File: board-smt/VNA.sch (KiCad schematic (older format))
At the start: 93 parts, among them J1 Conn_02x07_Odd_Even, J10 Conn_01x01, J11 Conn_01x01, J12 Conn_01x01, J13 Barrel_Jack, J14 Conn_01x01, J15 Conn_02x05_Odd_Even, J16 Conn_01x01, J17 Conn_01x04, J18 Conn_01x01, J19 Conn_01x01, J2 Conn_Coaxial, J20 Conn_01x01, J21 Conn_01x01, J22 Conn_01x02, J23 Conn_01x02, J24 USB_B, J25 Conn_01x02, J3 Conn_01x01, J4 Conn_01x01, J5 Conn_01x01, J6 Conn_01x01, J7 Conn_01x01, J8 Conn_01x01, J9 Conn_Coaxial, Q3 S9018, U1 SI5351A, U10 MT3608, U8 AMS1117-3V3, U9 78M05_TO252, Y1 27 MHz

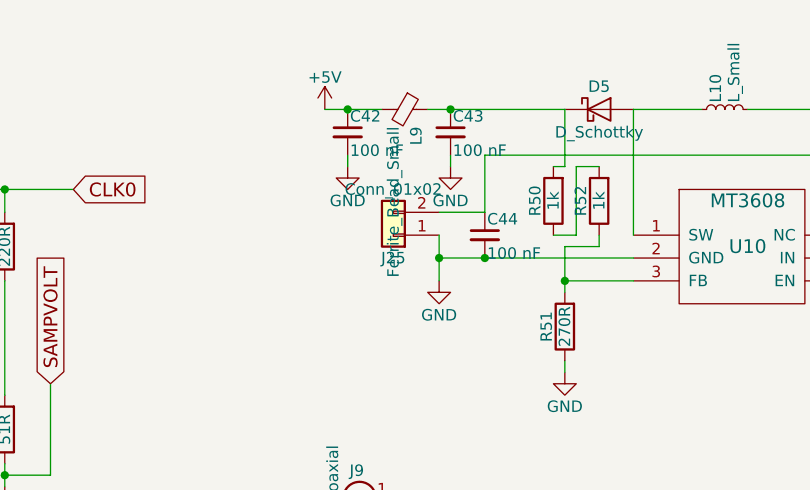
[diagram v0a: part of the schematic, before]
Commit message: 100 uH in pi filter
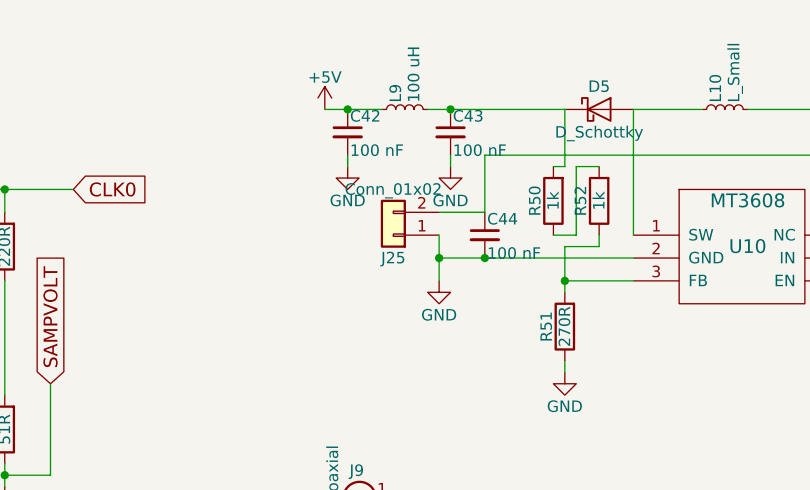
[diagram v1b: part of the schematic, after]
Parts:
- removed L9: Ferrite_Bead_Small, Inductors_SMD:L_1206_HandSoldering, symbol Ferrite_Bead_Small
- added L9: 100 uH, Inductors_SMD:L_1206_HandSoldering, symbol L_Small
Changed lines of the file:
@@
 Wire Wire Line
 	4800 800  5050 800
-$Comp
-L Ferrite_Bead_Small L9
-U 1 1 5DCD25CB
-P 5150 800
-F 0 "L9" H 5225 850 50  0000 L CNN
-F 1 "Ferrite_Bead_Small" H 5225 750 50  0000 L CNN
-F 2 "Inductors_SMD:L_1206_HandSoldering" V 5080 800 50  0001 C CNN
-F 3 "" H 5150 800 50  0001 C CNN
-	1    5150 800
-	0    1    1    0
-$EndComp
 Connection ~ 4900 800
 $Comp
@@
 	6000 1400 6000 1350
 Connection ~ 5850 1550
+$Comp
+L L_Small L9
+U 1 1 5DCCE487
+P 5150 800
+F 0 "L9" H 5180 840 50  0000 L CNN
+F 1 "100 uH" H 5180 760 50  0000 L CNN
+F 2 "Inductors_SMD:L_1206_HandSoldering" H 5150 800 50  0001 C CNN
+F 3 "" H 5150 800 50  0001 C CNN
+	1    5150 800
+	0    -1   -1   0
+$EndComp
 $EndSCHEMATC

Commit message: Rearranged the PCB, CN3502 battery charger and MT3608 boost converter on-board
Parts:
- removed C38, C44: 100 nF, Capacitors_SMD:C_0805_HandSoldering, symbol C_Small
- removed J15: Conn_02x05_Odd_Even, Pin_Headers:Pin_Header_Straight_2x05_Pitch2.54mm, symbol Conn_02x05_Odd_Even
- removed J25: Conn_01x02, Connectors_Molex:Molex_KK-6410-02_02x2.54mm_Straight, symbol Conn_01x02
- added C38, C44: 22 uF, Capacitors_SMD:CP_Elec_4x4.5, symbol CP
- added C45: 4.7 uF, Capacitors_SMD:CP_Elec_4x4.5, symbol CP
- added C49: 10 uF, Capacitors_SMD:CP_Elec_4x4.5, symbol CP
- added D6, D7: LED, LEDs:LED_0805, symbol LED
- added J15: Conn_01x03, Connectors_Molex:Molex_KK-6410-03_03x2.54mm_Straight, symbol Conn_01x03
- added JP6: Jumper_NC_Small, Pin_Headers:Pin_Header_Straight_1x02_Pitch2.54mm, symbol Jumper_NC_Small
- added R53: DIV1, Resistors_SMD:R_0805_HandSoldering, symbol R
- added R54: DIV2, Resistors_SMD:R_0805_HandSoldering, symbol R
- added R55: ISET, Resistors_SMD:R_0805_HandSoldering, symbol R
- added R56, R57: 270R, Resistors_SMD:R_0805_HandSoldering, symbol R
- added SW1: SW_DPDT_x2, Connectors_Molex:Molex_KK-6410-06_06x2.54mm_Straight, symbol SW_DPDT_x2
- added U11: CN3052, Housings_SOIC:SOIC-8_3.9x4.9mm_Pitch1.27mm, symbol CN3052
- L9: footprint Inductors_SMD:L_1206_HandSoldering -> Inductors_SMD:L_7.3x7.3_H4.5
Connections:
- net labels added: REG5VOUT
- wire segments 273 -> 304
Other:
- moved on the sheet: C42, C43, D3, D4, D5, J9, L10, L9, R17, R18, R50, R51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

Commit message: Move components around on board, adjusted fixture, added touchscreen disables
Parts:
- removed D6: LED, LEDs:LED_0805, symbol LED
- removed J15: Conn_01x03, Connectors_Molex:Molex_KK-6410-03_03x2.54mm_Straight, symbol Conn_01x03
- removed J23: Conn_01x02, Connectors_Molex:Molex_KK-6410-02_02x2.54mm_Straight, symbol Conn_01x02
- removed R54: DIV2, Resistors_SMD:R_0805_HandSoldering, symbol R
- removed R56: 270R, Resistors_SMD:R_0805_HandSoldering, symbol R
- added J15: Conn_01x02, Connectors_Molex:Molex_KK-6410-02_02x2.54mm_Straight, symbol Conn_01x02
- R53: value DIV1 -> 10k
- R55: value ISET -> 4k7
- Y1: footprint Crystals:Crystal_HC49-U_Vertical -> Crystals:Crystal_SMD_3225-4pin_3.2x2.5mm_HandSoldering
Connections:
- net labels added: POWFILT
- wire segments 304 -> 291
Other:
- moved on the sheet: C42, C43, L9

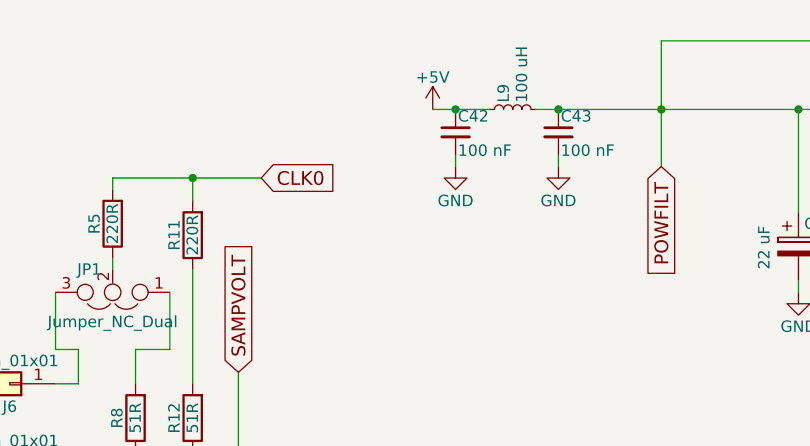
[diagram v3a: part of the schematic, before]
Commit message: Added protection Zener diode on Pi filter to protect against ON/OFF transients
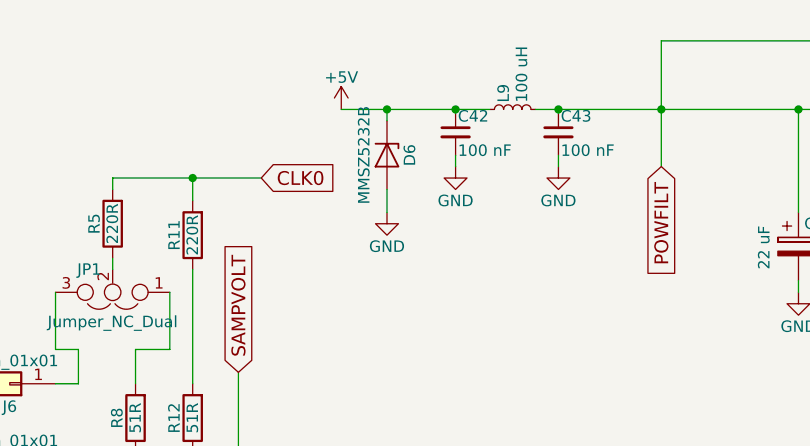
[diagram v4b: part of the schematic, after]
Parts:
- added D6: MMSZ5232B, Diodes_SMD:D_SOD-123, symbol D_Zener
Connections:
- net +5V: now also D6.1 (K)
- net GND: now also D6.2 (A)
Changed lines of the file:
@@
 $EndComp
 $Comp
-L +3V3 #PWR35
+L +3V3 #PWR36
 U 1 1 5BB1752D
 P 5700 5700
-F 0 "#PWR35" H 5700 5550 50  0001 C CNN
+F 0 "#PWR36" H 5700 5550 50  0001 C CNN
 F 1 "+3V3" H 5700 5840 50  0000 C CNN
 F 2 "" H 5700 5700 50  0001 C CNN
@@
 SYNCSAMPLE
 $Comp
-L +5V #PWR55
+L +5V #PWR56
 U 1 1 5BB2CE22
 P 9550 4200
-F 0 "#PWR55" H 9550 4050 50  0001 C CNN
+F 0 "#PWR56" H 9550 4050 50  0001 C CNN
 F 1 "+5V" H 9550 4340 50  0000 C CNN
 F 2 "" H 9550 4200 50  0001 C CNN
@@
 $EndComp
 $Comp
-L GND #PWR38
+L GND #PWR39
 U 1 1 5BB2D2D6
 P 6000 6000
-F 0 "#PWR38" H 6000 5750 50  0001 C CNN
+F 0 "#PWR39" H 6000 5750 50  0001 C CNN
 F 1 "GND" H 6000 5850 50  0000 C CNN
 F 2 "" H 6000 6000 50  0001 C CNN
@@
 $EndComp
 $Comp
-L GND #PWR36
+L GND #PWR37
 U 1 1 5BB350C1
 P 5750 3400
-F 0 "#PWR36" H 5750 3150 50  0001 C CNN
+F 0 "#PWR37" H 5750 3150 50  0001 C CNN
 F 1 "GND" H 5750 3250 50  0000 C CNN
 F 2 "" H 5750 3400 50  0001 C CNN
@@
 $EndComp
 $Comp
-L +5V #PWR59
+L +5V #PWR60
 U 1 1 5BB3F764
 P 10550 5200
-F 0 "#PWR59" H 10550 5050 50  0001 C CNN
+F 0 "#PWR60" H 10550 5050 50  0001 C CNN
 F 1 "+5V" H 10550 5340 50  0000 C CNN
 F 2 "" H 10550 5200 50  0001 C CNN
@@
 $EndComp
 $Comp
-L GND #PWR61
+L GND #PWR62
 U 1 1 5BB3F96D
 P 10850 5900
-F 0 "#PWR61" H 10850 5650 50  0001 C CNN
+F 0 "#PWR62" H 10850 5650 50  0001 C CNN
 F 1 "GND" H 10850 5750 50  0000 C CNN
 F 2 "" H 10850 5900 50  0001 C CNN
@@
 $EndComp
 $Comp
-L GND #PWR62
+L GND #PWR63
 U 1 1 5BB37FFB
 P 11200 4650
-F 0 "#PWR62" H 11200 4400 50  0001 C CNN
+F 0 "#PWR63" H 11200 4400 50  0001 C CNN
 F 1 "GND" H 11200 4500 50  0000 C CNN
 F 2 "" H 11200 4650 50  0001 C CNN
@@
 $EndComp
 $Comp
-L +5V #PWR56
+L +5V #PWR57
 U 1 1 5BB381D0
 P 10100 2650
-F 0 "#PWR56" H 10100 2500 50  0001 C CNN
+F 0 "#PWR57" H 10100 2500 50  0001 C CNN
 F 1 "+5V" H 10100 2790 50  0000 C CNN
 F 2 "" H 10100 2650 50  0001 C CNN
@@
 $EndComp
 $Comp
-L GND #PWR32
+L GND #PWR33
 U 1 1 5BE16D13
 P 4800 3050
-F 0 "#PWR32" H 4800 2800 50  0001 C CNN
+F 0 "#PWR33" H 4800 2800 50  0001 C CNN
 F 1 "GND" H 4800 2900 50  0000 C CNN
 F 2 "" H 4800 3050 50  0001 C CNN
@@
 $EndComp
 $Comp
-L GND #PWR27
+L GND #PWR28
 U 1 1 5BFEB64E
 P 4050 5600
-F 0 "#PWR27" H 4050 5350 50  0001 C CNN
+F 0 "#PWR28" H 4050 5350 50  0001 C CNN
 F 1 "GND" H 4050 5450 50  0000 C CNN
 F 2 "" H 4050 5600 50  0001 C CNN
@@
 $EndComp
 $Comp
-L GND #PWR31
+L GND #PWR32
 U 1 1 5BFEBC91
 P 4750 5600
-F 0 "#PWR31" H 4750 5350 50  0001 C CNN
+F 0 "#PWR32" H 4750 5350 50  0001 C CNN
 F 1 "GND" H 4750 5450 50  0000 C CNN
 F 2 "" H 4750 5600 50  0001 C CNN
@@
 $EndComp
 $Comp
-L GND #PWR34
+L GND #PWR35
 U 1 1 5C1BDCBD
 P 5150 6200
-F 0 "#PWR34" H 5150 5950 50  0001 C CNN
+F 0 "#PWR35" H 5150 5950 50  0001 C CNN
 F 1 "GND" H 5150 6050 50  0000 C CNN
 F 2 "" H 5150 6200 50  0001 C CNN
@@
 $EndComp
 $Comp
-L GND #PWR53
+L GND #PWR54
 U 1 1 5C258D29
 P 9350 3900
-F 0 "#PWR53" H 9350 3650 50  0001 C CNN
+F 0 "#PWR54" H 9350 3650 50  0001 C CNN
 F 1 "GND" H 9350 3750 50  0000 C CNN
 F 2 "" H 9350 3900 50  0001 C CNN
@@
 $EndComp
 $Comp
-L GND #PWR37
+L GND #PWR38
 U 1 1 5C25906A
 P 5800 6050
-F 0 "#PWR37" H 5800 5800 50  0001 C CNN
+F 0 "#PWR38" H 5800 5800 50  0001 C CNN
 F 1 "GND" H 5800 5900 50  0000 C CNN
 F 2 "" H 5800 6050 50  0001 C CNN
@@
 $EndComp
 $Comp
-L GND #PWR50
+L GND #PWR51
 U 1 1 5D1ABD6C
 P 9150 3400
-F 0 "#PWR50" H 9150 3150 50  0001 C CNN
+F 0 "#PWR51" H 9150 3150 50  0001 C CNN
 F 1 "GND" H 9150 3250 50  0000 C CNN
 F 2 "" H 9150 3400 50  0001 C CNN
@@
 $EndComp
 $Comp
-L +5V #PWR49
+L +5V #PWR50
 U 1 1 5D1AC0C3
 P 8800 2900
-F 0 "#PWR49" H 8800 2750 50  0001 C CNN
+F 0 "#PWR50" H 8800 2750 50  0001 C CNN
 F 1 "+5V" H 8800 3040 50  0000 C CNN
 F 2 "" H 8800 2900 50  0001 C CNN
@@
 $EndComp
 $Comp
-L GND #PWR54
+L GND #PWR55
 U 1 1 5D1ACA17
 P 9550 3650
-F 0 "#PWR54" H 9550 3400 50  0001 C CNN
+F 0 "#PWR55" H 9550 3400 50  0001 C CNN
 F 1 "GND" H 9550 3500 50  0000 C CNN
 F 2 "" H 9550 3650 50  0001 C CNN
@@
 $EndComp
 $Comp
-L GND #PWR29
+L GND #PWR30
 U 1 1 5D91A3E2
 P 4450 6550
-F 0 "#PWR29" H 4450 6300 50  0001 C CNN
+F 0 "#PWR30" H 4450 6300 50  0001 C CNN
 F 1 "GND" H 4450 6400 50  0000 C CNN
 F 2 "" H 4450 6550 50  0001 C CNN
@@
 NoConn ~ 10350 4350
 $Comp
-L +5V #PWR58
+L +5V #PWR59
 U 1 1 5DB1C7B8
 P 10200 4500
-F 0 "#PWR58" H 10200 4350 50  0001 C CNN
+F 0 "#PWR59" H 10200 4350 50  0001 C CNN
 F 1 "+5V" H 10200 4640 50  0000 C CNN
 F 2 "" H 10200 4500 50  0001 C CNN
@@
 $EndComp
 $Comp
-L GND #PWR48
+L GND #PWR49
 U 1 1 5DCC5E0A
 P 8650 6300
-F 0 "#PWR48" H 8650 6050 50  0001 C CNN
+F 0 "#PWR49" H 8650 6050 50  0001 C CNN
 F 1 "GND" H 8650 6150 50  0000 C CNN
 F 2 "" H 8650 6300 50  0001 C CNN
@@
 $EndComp
 $Comp
-L GND #PWR60
+L GND #PWR61
 U 1 1 5DCC6B2E
 P 10600 6450
-F 0 "#PWR60" H 10600 6200 50  0001 C CNN
+F 0 "#PWR61" H 10600 6200 50  0001 C CNN
 F 1 "GND" H 10600 6300 50  0000 C CNN
 F 2 "" H 10600 6450 50  0001 C CNN
@@
 $EndComp
 $Comp
-L GND #PWR33
+L GND #PWR34
 U 1 1 5DCD10CA
 P 5000 1100
-F 0 "#PWR33" H 5000 850 50  0001 C CNN
+F 0 "#PWR34" H 5000 850 50  0001 C CNN
 F 1 "GND" H 5000 950 50  0000 C CNN
 F 2 "" H 5000 1100 50  0001 C CNN
@@
 $EndComp
 $Comp
-L +5V #PWR28
+L +5V #PWR27
 U 1 1 5DCD163E
-P 4450 850
-F 0 "#PWR28" H 4450 700 50  0001 C CNN
-F 1 "+5V" H 4450 990 50  0000 C CNN
-F 2 "" H 4450 850 50  0001 C CNN
-F 3 "" H 4450 850 50  0001 C CNN
-	1    4450 850
+P 4050 850
+F 0 "#PWR27" H 4050 700 50  0001 C CNN
+F 1 "+5V" H 4050 990 50  0000 C CNN
+F 2 "" H 4050 850 50  0001 C CNN
+F 3 "" H 4050 850 50  0001 C CNN
+	1    4050 850
 	1    0    0    -1
 $EndComp
@@
 $EndComp
 $Comp
-L GND #PWR30
+L GND #PWR31
 U 1 1 5DCD1D7F
 P 4550 1100
-F 0 "#PWR30" H 4550 850 50  0001 C CNN
+F 0 "#PWR31" H 4550 850 50  0001 C CNN
 F 1 "GND" H 4550 950 50  0000 C CNN
 F 2 "" H 4550 1100 50  0001 C CNN
@@
 $EndComp
 $Comp
-L GND #PWR46
+L GND #PWR47
 U 1 1 5DCDAD80
 P 8100 1300
-F 0 "#PWR46" H 8100 1050 50  0001 C CNN
+F 0 "#PWR47" H 8100 1050 50  0001 C CNN
 F 1 "GND" H 8100 1150 50  0000 C CNN
 F 2 "" H 8100 1300 50  0001 C CNN
@@
 $EndComp
 $Comp
-L GND #PWR40
+L GND #PWR41
 U 1 1 5DCDB2D2
 P 6450 2000
-F 0 "#PWR40" H 6450 1750 50  0001 C CNN
+F 0 "#PWR41" H 6450 1750 50  0001 C CNN
 F 1 "GND" H 6450 1850 50  0000 C CNN
 F 2 "" H 6450 2000 50  0001 C CNN
@@
 $EndComp
 $Comp
-L GND #PWR39
+L GND #PWR40
 U 1 1 5DCDC2A3
 P 6050 1650
-F 0 "#PWR39" H 6050 1400 50  0001 C CNN
+F 0 "#PWR40" H 6050 1400 50  0001 C CNN
 F 1 "GND" H 6050 1500 50  0000 C CNN
 F 2 "" H 6050 1650 50  0001 C CNN
@@
 $EndComp
 $Comp
-L GND #PWR41
+L GND #PWR42
 U 1 1 5DCD9C13
 P 6650 1700
-F 0 "#PWR41" H 6650 1450 50  0001 C CNN
+F 0 "#PWR42" H 6650 1450 50  0001 C CNN
 F 1 "GND" H 6650 1550 50  0000 C CNN
 F 2 "" H 6650 1700 50  0001 C CNN
@@
 $EndComp
 $Comp
-L GND #PWR52
+L GND #PWR53
 U 1 1 5DCDDC50
 P 9350 1500
-F 0 "#PWR52" H 9350 1250 50  0001 C CNN
+F 0 "#PWR53" H 9350 1250 50  0001 C CNN
 F 1 "GND" H 9350 1350 50  0000 C CNN
 F 2 "" H 9350 1500 50  0001 C CNN
@@
 $EndComp
 $Comp
-L GND #PWR51
+L GND #PWR52
 U 1 1 5DCE11B6
 P 9250 2150
-F 0 "#PWR51" H 9250 1900 50  0001 C CNN
+F 0 "#PWR52" H 9250 1900 50  0001 C CNN
 F 1 "GND" H 9250 2000 50  0000 C CNN
 F 2 "" H 9250 2150 50  0001 C CNN
@@
 $EndComp
 $Comp
-L GND #PWR43
+L GND #PWR44
 U 1 1 5DCE3E90
 P 6900 2850
-F 0 "#PWR43" H 6900 2600 50  0001 C CNN
+F 0 "#PWR44" H 6900 2600 50  0001 C CNN
 F 1 "GND" H 6900 2700 50  0000 C CNN
 F 2 "" H 6900 2850 50  0001 C CNN
@@
 $EndComp
 $Comp
-L GND #PWR44
+L GND #PWR45
 U 1 1 5DCE425A
 P 7150 2850
-F 0 "#PWR44" H 7150 2600 50  0001 C CNN
+F 0 "#PWR45" H 7150 2600 50  0001 C CNN
 F 1 "GND" H 7150 2700 50  0000 C CNN
 F 2 "" H 7150 2850 50  0001 C CNN
@@
 $EndComp
 $Comp
-L GND #PWR47
+L GND #PWR48
 U 1 1 5DCE4711
 P 8400 3150
-F 0 "#PWR47" H 8400 2900 50  0001 C CNN
+F 0 "#PWR48" H 8400 2900 50  0001 C CNN
 F 1 "GND" H 8400 3000 50  0000 C CNN
 F 2 "" H 8400 3150 50  0001 C CNN
@@
 $EndComp
 $Comp
-L GND #PWR42
+L GND #PWR43
 U 1 1 5DCE9CC0
 P 6700 2850
-F 0 "#PWR42" H 6700 2600 50  0001 C CNN
+F 0 "#PWR43" H 6700 2600 50  0001 C CNN
 F 1 "GND" H 6700 2700 50  0000 C CNN
 F 2 "" H 6700 2850 50  0001 C CNN
@@
 $EndComp
 $Comp
-L +3V3 #PWR57
+L +3V3 #PWR58
 U 1 1 5DCECE37
 P 10150 6400
-F 0 "#PWR57" H 10150 6250 50  0001 C CNN
+F 0 "#PWR58" H 10150 6250 50  0001 C CNN
 F 1 "+3V3" H 10150 6540 50  0000 C CNN
 F 2 "" H 10150 6400 50  0001 C CNN
@@
 Connection ~ 4550 850
 Wire Wire Line
-	4450 850  4700 850
+	4050 850  4700 850
 Wire Wire Line
 	4550 1100 4550 1050
@@
 $EndComp
 $Comp
-L GND #PWR45
+L GND #PWR46
 U 1 1 5DCFBBCA
 P 7650 1250
-F 0 "#PWR45" H 7650 1000 50  0001 C CNN
+F 0 "#PWR46" H 7650 1000 50  0001 C CNN
 F 1 "GND" H 7650 1100 50  0000 C CNN
 F 2 "" H 7650 1250 50  0001 C CNN
@@
 	7650 900  7650 850
 Connection ~ 7650 850
+$Comp
+L D_Zener D6
+U 1 1 5DD11059
+P 4250 1050
+F 0 "D6" H 4250 1150 50  0000 C CNN
+F 1 "MMSZ5232B" H 4250 950 50  0000 C CNN
+F 2 "Diodes_SMD:D_SOD-123" H 4250 1050 50  0001 C CNN
+F 3 "" H 4250 1050 50  0001 C CNN
+	1    4250 1050
+	0    1    1    0
+$EndComp
+$Comp
+L GND #PWR29
+U 1 1 5DD11212
+P 4250 1300
+F 0 "#PWR29" H 4250 1050 50  0001 C CNN
+F 1 "GND" H 4250 1150 50  0000 C CNN
+F 2 "" H 4250 1300 50  0001 C CNN
+F 3 "" H 4250 1300 50  0001 C CNN
+	1    4250 1300
+	1    0    0    -1
+$EndComp
+Wire Wire Line
+	4250 1300 4250 1200
+Wire Wire Line
+	4250 900  4250 850
+Connection ~ 4250 850
 $EndSCHEMATC
